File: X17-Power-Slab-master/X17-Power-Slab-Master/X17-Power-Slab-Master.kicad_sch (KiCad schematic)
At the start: 18 parts, among them J2 ET60S-D04-3-08-D04-X-R1-S, J3 796636-6, Q1 NMOS, U1 AZ1117IH-3.3TRG1

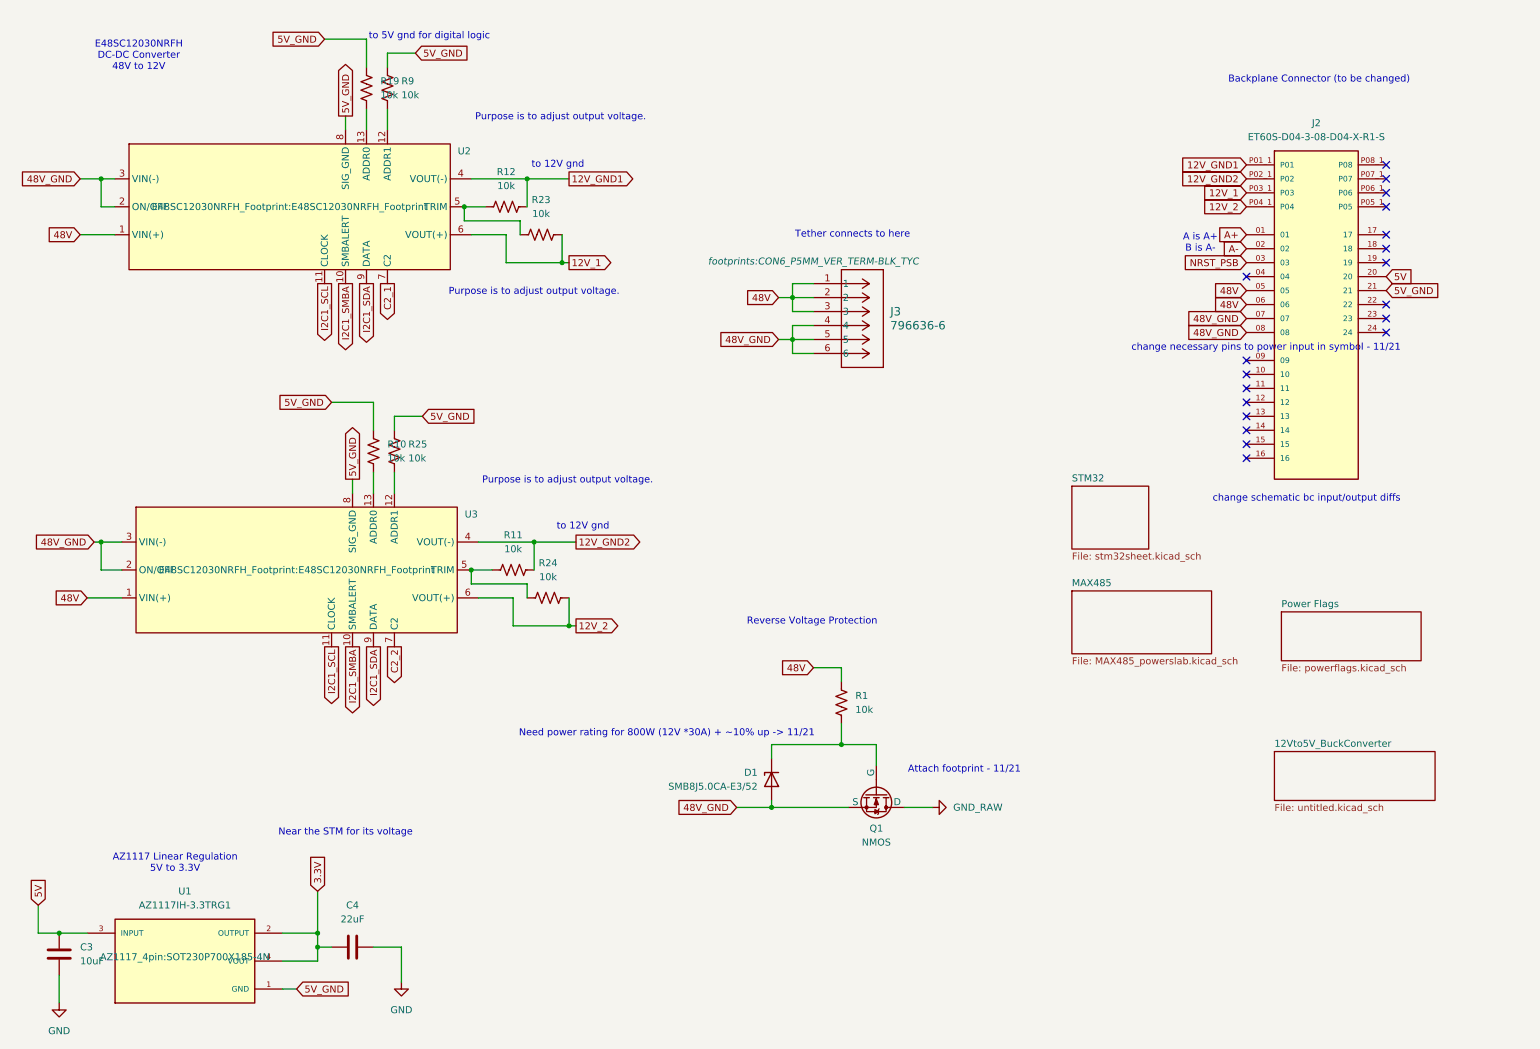
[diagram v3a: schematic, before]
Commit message: Initial Placements
Issue - NRST_PSB is apparently ground flag
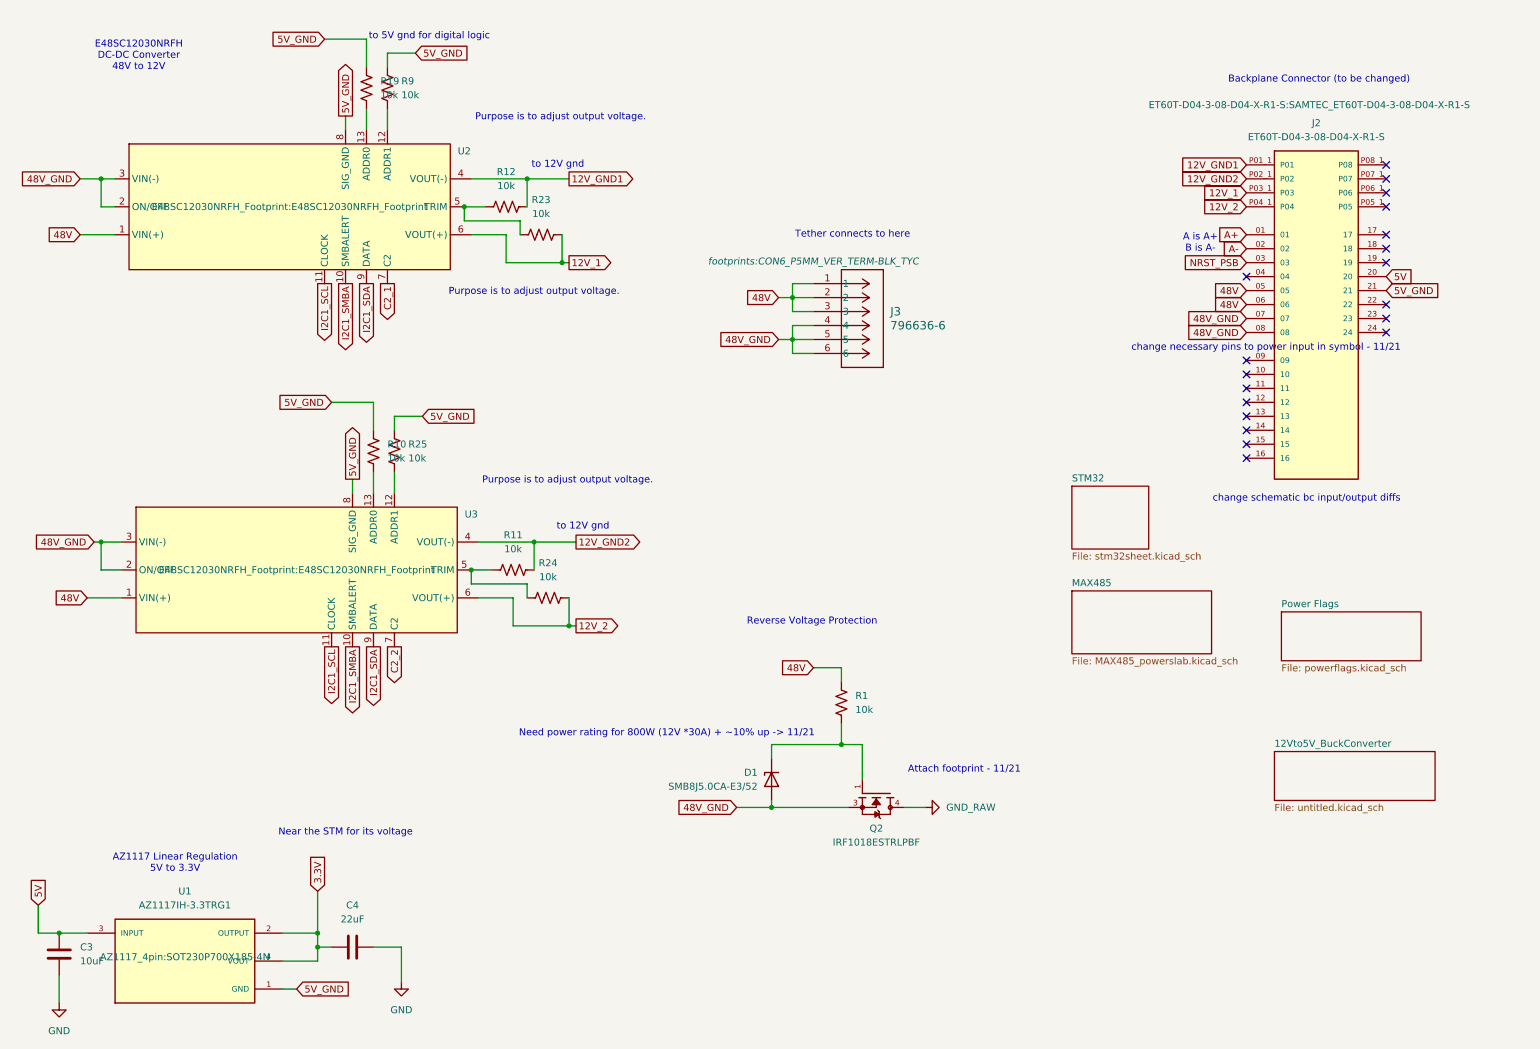
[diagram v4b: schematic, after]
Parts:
- removed Q1: NMOS, Reverse Voltage Protection:TO254P1524X483-4, symbol Simulation_SPICE:NMOS
- added Q2: IRF1018ESTRLPBF, Reverse Voltage Protection:TO254P1524X483-4, symbol IRF1018ESTRLPBF:IRF1018ESTRLPBF
- J2: value ET60S-D04-3-08-D04-X-R1-S -> ET60T-D04-3-08-D04-X-R1-S; footprint ET60S-D04-3-08-D04-X-R1-S:SAMTEC_ET60S-D04-3-08-D04-X-R1-S -> ET60T-D04-3-08-D04-X-R1-S:SAMTEC_ET60T-D04-3-08-D04-X-R1-S
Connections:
- net 48V_GND: now also Q2.3
- net GND_RAW: now also Q2.4
- net at D1.1 (K), R1.2: now also Q2.1
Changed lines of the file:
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@@
+	)
+	(junction
+		(at 166.37 143.51)
+		(diameter 0)
+		(color 0 0 0 0)
 	)
 	(junction
@@
 	)
 	(junction
-		(at 166.37 143.51)
-		(diameter 0)
-		(color 0 0 0 0)
-	)
-	(junction
 		(at 116.84 121.92)
 		(diameter 0)
@@
 	(wire
 		(pts
+			(xy 166.37 143.51) (xy 170.18 143.51)
+		)
+		(stroke
+			(width 0)
+			(type default)
+		)
+	)
+	(wire
+		(pts
 			(xy 73.66 81.28) (xy 81.28 81.28)
 		)
@@
 	(wire
 		(pts
-			(xy 172.72 147.32) (xy 172.72 143.51)
-		)
-		(stroke
-			(width 0)
-			(type default)
-		)
-	)
-	(wire
-		(pts
 			(xy 31.75 40.64) (xy 34.29 40.64)
 		)
@@
 	(wire
 		(pts
+			(xy 177.8 154.94) (xy 181.61 154.94)
+		)
+		(stroke
+			(width 0)
+			(type default)
+		)
+	)
+	(wire
+		(pts
 			(xy 80.01 20.32) (xy 80.01 15.24)
 		)
@@
 	(wire
 		(pts
-			(xy 177.8 154.94) (xy 182.88 154.94)
-		)
-		(stroke
-			(width 0)
-			(type default)
-		)
-	)
-	(wire
-		(pts
 			(xy 24.13 177.8) (xy 20.32 177.8)
 		)
@@
 	(wire
 		(pts
-			(xy 172.72 143.51) (xy 166.37 143.51)
-		)
-		(stroke
-			(width 0)
-			(type default)
-		)
-	)
-	(wire
-		(pts
 			(xy 106.68 121.92) (xy 116.84 121.92)
 		)
@@
 		(pts
 			(xy 72.39 15.24) (xy 80.01 15.24)
+		)
+		(stroke
+			(width 0)
+			(type default)
+		)
+	)
+	(wire
+		(pts
+			(xy 170.18 143.51) (xy 170.18 149.86)
 		)
 		(stroke
@@
 			)
 		)
-		(property "Value" "ET60S-D04-3-08-D04-X-R1-S"
+		(property "Value" "ET60T-D04-3-08-D04-X-R1-S"
 			(at 252.73 33.02 0)
 			(effects
@@
 			)
 		)
-		(property "Footprint" "ET60S-D04-3-08-D04-X-R1-S:SAMTEC_ET60S-D04-3-08-D04-X-R1-S"
+		(property "Footprint" "ET60T-D04-3-08-D04-X-R1-S:SAMTEC_ET60T-D04-3-08-D04-X-R1-S"
 			(at 251.46 27.94 0)
 			(effects
@@
 				)
 				(justify bottom)
-				(hide yes)
 			)
 		)
@@
 	)
 	(symbol
+		(lib_id "IRF1018ESTRLPBF:IRF1018ESTRLPBF")
+		(at 172.72 152.4 270)
+		(unit 1)
+		(exclude_from_sim no)
+		(in_bom yes)
+		(on_board yes)
+		(dnp no)
+		(fields_autoplaced yes)
+		(property "Reference" "Q2"
+			(at 172.72 158.75 90)
+			(effects
+				(font
+					(size 1.27 1.27)
+				)
+			)
+		)
+		(property "Value" "IRF1018ESTRLPBF"
+			(at 172.72 161.29 90)
+			(effects
+				(font
+					(size 1.27 1.27)
+				)
+			)
+		)
+		(property "Footprint" "Reverse Voltage Protection:TO254P1524X483-4"
+			(at 172.72 152.4 0)
+			(effects
+				(font
+					(size 1.27 1.27)
+				)
+				(justify bottom)
+				(hide yes)
+			)
+		)
+		(property "Datasheet" ""
+			(at 172.72 152.4 0)
+			(effects
+				(font
+					(size 1.27 1.27)
+				)
+				(hide yes)
+			)
+		)
+		(property "Description" ""
+			(at 172.72 152.4 0)
+			(effects
+				(font
+					(size 1.27 1.27)
+				)
+				(hide yes)
+			)
+		)
+		(property "SNAPEDA_PACKAGE_ID" "22196"
+			(at 172.72 152.4 0)
+			(effects
+				(font
+					(size 1.27 1.27)
+				)
+				(justify bottom)
+				(hide yes)
+			)
+		)
+		(property "MAXIMUM_PACKAGE_HEIGHT" "4.83 mm"
+			(at 172.72 152.4 0)
+			(effects
+				(font
+					(size 1.27 1.27)
+				)
+				(justify bottom)
+				(hide yes)
+			)
+		)
+		(property "STANDARD" "IPC 7351B"
+			(at 172.72 152.4 0)
+			(effects
+				(font
+					(size 1.27 1.27)
+				)
+				(justify bottom)
+				(hide yes)
+			)
+		)
+		(property "PARTREV" "03/16/07"
+			(at 172.72 152.4 0)
+			(effects
+				(font
+					(size 1.27 1.27)
+				)
+				(justify bottom)
+				(hide yes)
+			)
+		)
+		(property "SNAPEDA_PN" "IRF1018ESTRLPBF"
+			(at 172.72 152.4 0)
+			(effects
+				(font
+					(size 1.27 1.27)
+				)
+				(justify bottom)
+				(hide yes)
+			)
+		)
+		(property "MANUFACTURER" "Infineon"
+			(at 172.72 152.4 0)
+			(effects
+				(font
+					(size 1.27 1.27)
+				)
+				(justify bottom)
+				(hide yes)
+			)
+		)
+		(pin "1"
+		)
+		(pin "3"
+		)
+		(pin "4"
+		)
+		(instances
+			(project ""
+				(path "/57e59c68-7be1-495e-b535-e78e0f561e15"
+					(reference "Q2")
+					(unit 1)
+				)
+			)
+		)
+	)
+	(symbol
 		(lib_id "Device:R_US")
 		(at 106.68 111.76 90)
@@
 	)
 	(symbol
-		(lib_id "Simulation_SPICE:NMOS")
-		(at 172.72 152.4 270)
+		(lib_id "power:GND")
+		(at 181.61 154.94 90)
 		(unit 1)
 		(exclude_from_sim no)
@@
 		(dnp no)
 		(fields_autoplaced yes)
-		(property "Reference" "Q1"
-			(at 172.72 158.75 90)
-			(effects
-				(font
-					(size 1.27 1.27)
-				)
-			)
-		)
-		(property "Value" "NMOS"
-			(at 172.72 161.29 90)
-			(effects
-				(font
-					(size 1.27 1.27)
-				)
-			)
-		)
-		(property "Footprint" "Reverse Voltage Protection:TO254P1524X483-4"
-			(at 175.26 157.48 0)
-			(effects
-				(font
-					(size 1.27 1.27)
-				)
-				(hide yes)
-			)
-		)
-		(property "Datasheet" "https://www.infineon.com/dgdl/irf1018epbf.pdf?fileId=5546d462533600a4015355da854e1891"
-			(at 160.02 152.4 0)
-			(effects
-				(font
-					(size 1.27 1.27)
-				)
-				(hide yes)
-			)
-		)
-		(property "Description" "N-MOSFET transistor, drain/source/gate"
-			(at 172.72 152.4 0)
-			(effects
-				(font
-					(size 1.27 1.27)
-				)
-				(hide yes)
-			)
-		)
-		(property "Sim.Device" "NMOS"
-			(at 155.575 152.4 0)
-			(effects
-				(font
-					(size 1.27 1.27)
-				)
-				(hide yes)
-			)
-		)
-		(property "Sim.Type" "VDMOS"
-			(at 153.67 152.4 0)
-			(effects
-				(font
-					(size 1.27 1.27)
-				)
-				(hide yes)
-			)
-		)
-		(property "Sim.Pins" "1=D 2=G 3=S"
-			(at 157.48 152.4 0)
-			(effects
-				(font
-					(size 1.27 1.27)
-				)
-				(hide yes)
-			)
-		)
-		(pin "3"
-		)
-		(pin "1"
-		)
-		(pin "2"
-		)
-		(instances
-			(project ""
-				(path "/57e59c68-7be1-495e-b535-e78e0f561e15"
-					(reference "Q1")
-					(unit 1)
-				)
-			)
-		)
-	)
-	(symbol
-		(lib_id "power:GND")
-		(at 182.88 154.94 90)
-		(unit 1)
-		(exclude_from_sim no)
-		(in_bom yes)
-		(on_board yes)
-		(dnp no)
-		(fields_autoplaced yes)
 		(property "Reference" "#PWR07"
-			(at 189.23 154.94 0)
+			(at 187.96 154.94 0)
 			(effects
 				(font
@@
 		)
 		(property "Value" "GND_RAW"
-			(at 186.69 154.9399 90)
+			(at 185.42 154.9399 90)
 			(effects
 				(font
@@
 		)
 		(property "Footprint" ""
-			(at 182.88 154.94 0)
+			(at 181.61 154.94 0)
 			(effects
 				(font
@@
 		)
 		(property "Datasheet" ""
-			(at 182.88 154.94 0)
+			(at 181.61 154.94 0)
 			(effects
 				(font
@@
 		)
 		(property "Description" "Power symbol creates a global label with name \"GND\" , ground"
-			(at 182.88 154.94 0)
-			(effects
-				(font
+			(at 181.61 154.94 0)
+			(effects
+				(font
